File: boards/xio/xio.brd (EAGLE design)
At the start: 170 x 170 mm, 390 parts, among them U2 LAN8742A-CZ, Y1 NX3225SA-12.000MHZ-STD-CSR-1, Y2 NX3225SA-12.000MHZ-STD-CSR-1, Y3 NX3225SA-25.000MHZ-STD-CSR-1

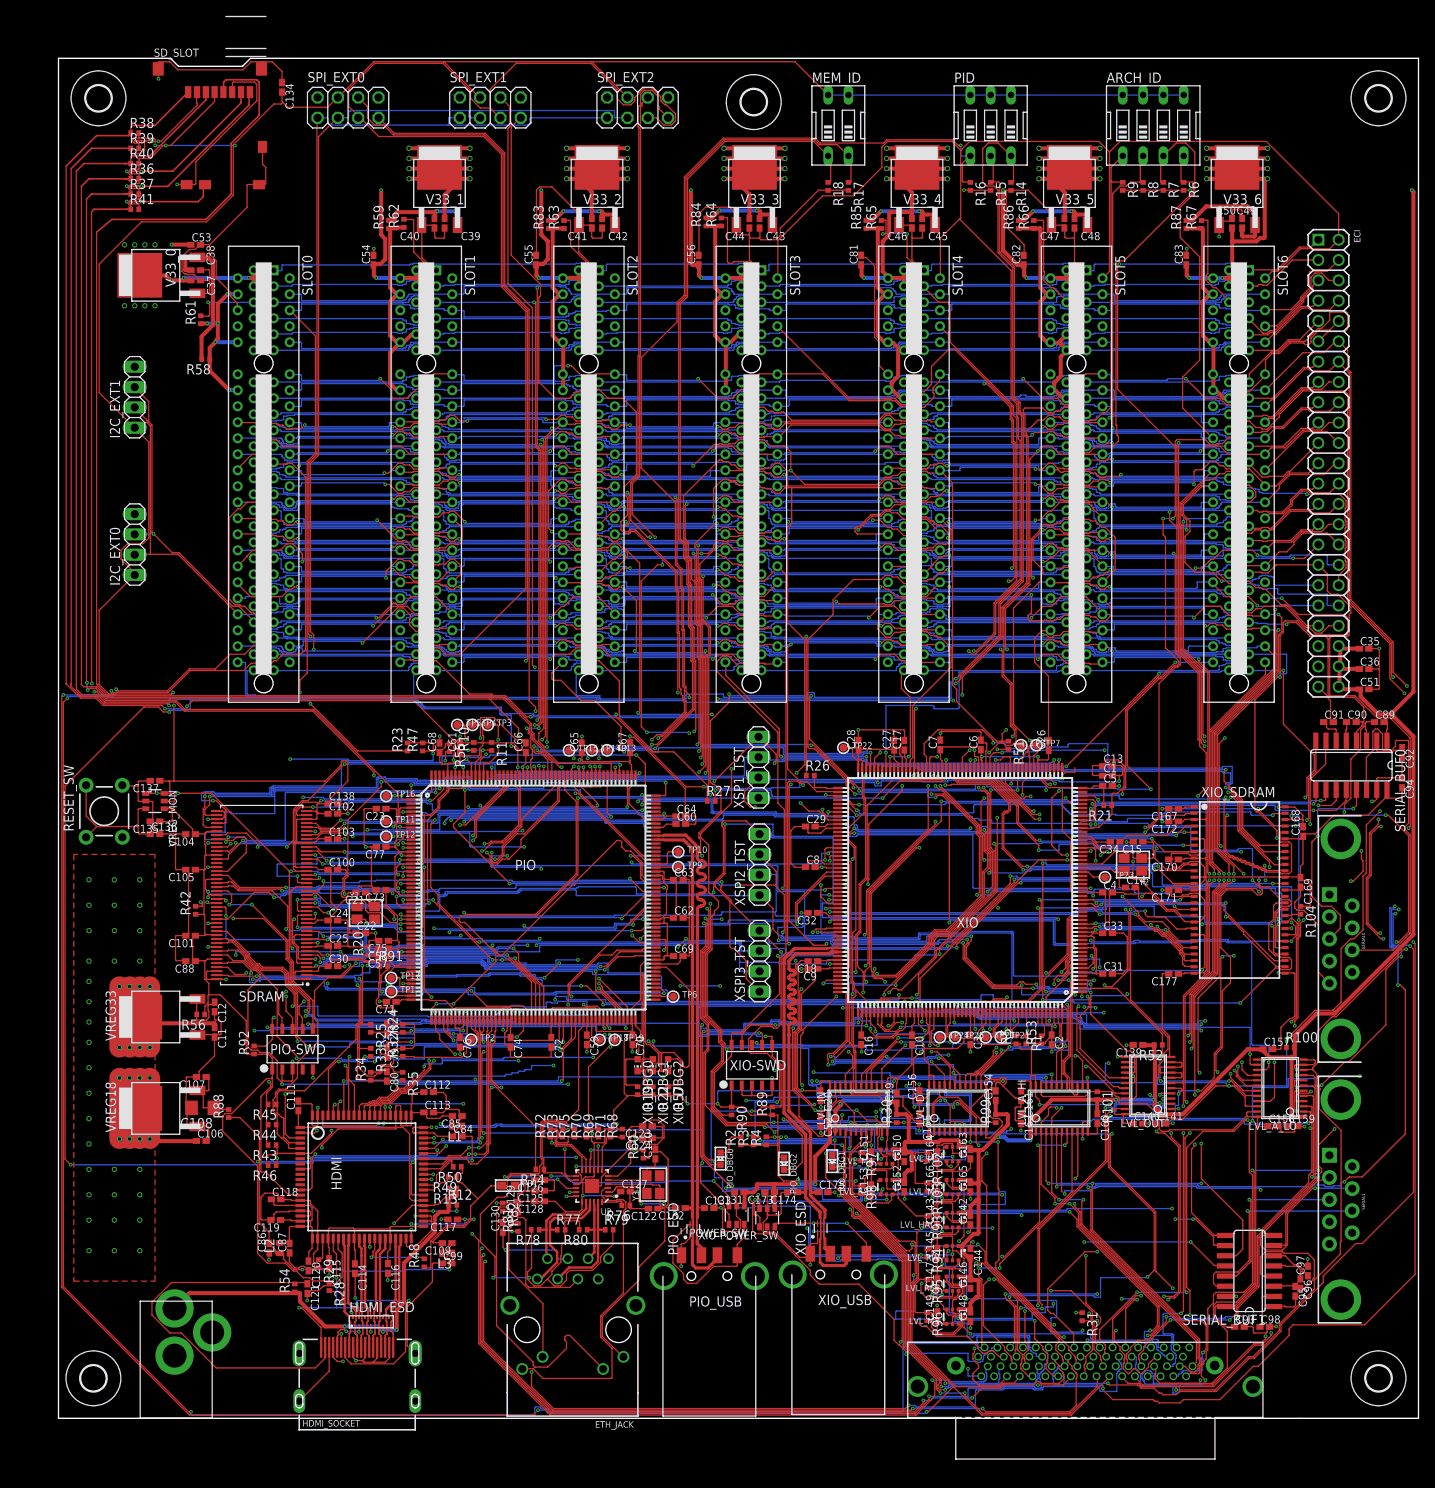
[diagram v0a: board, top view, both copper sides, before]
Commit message: Move to a 6-layer board
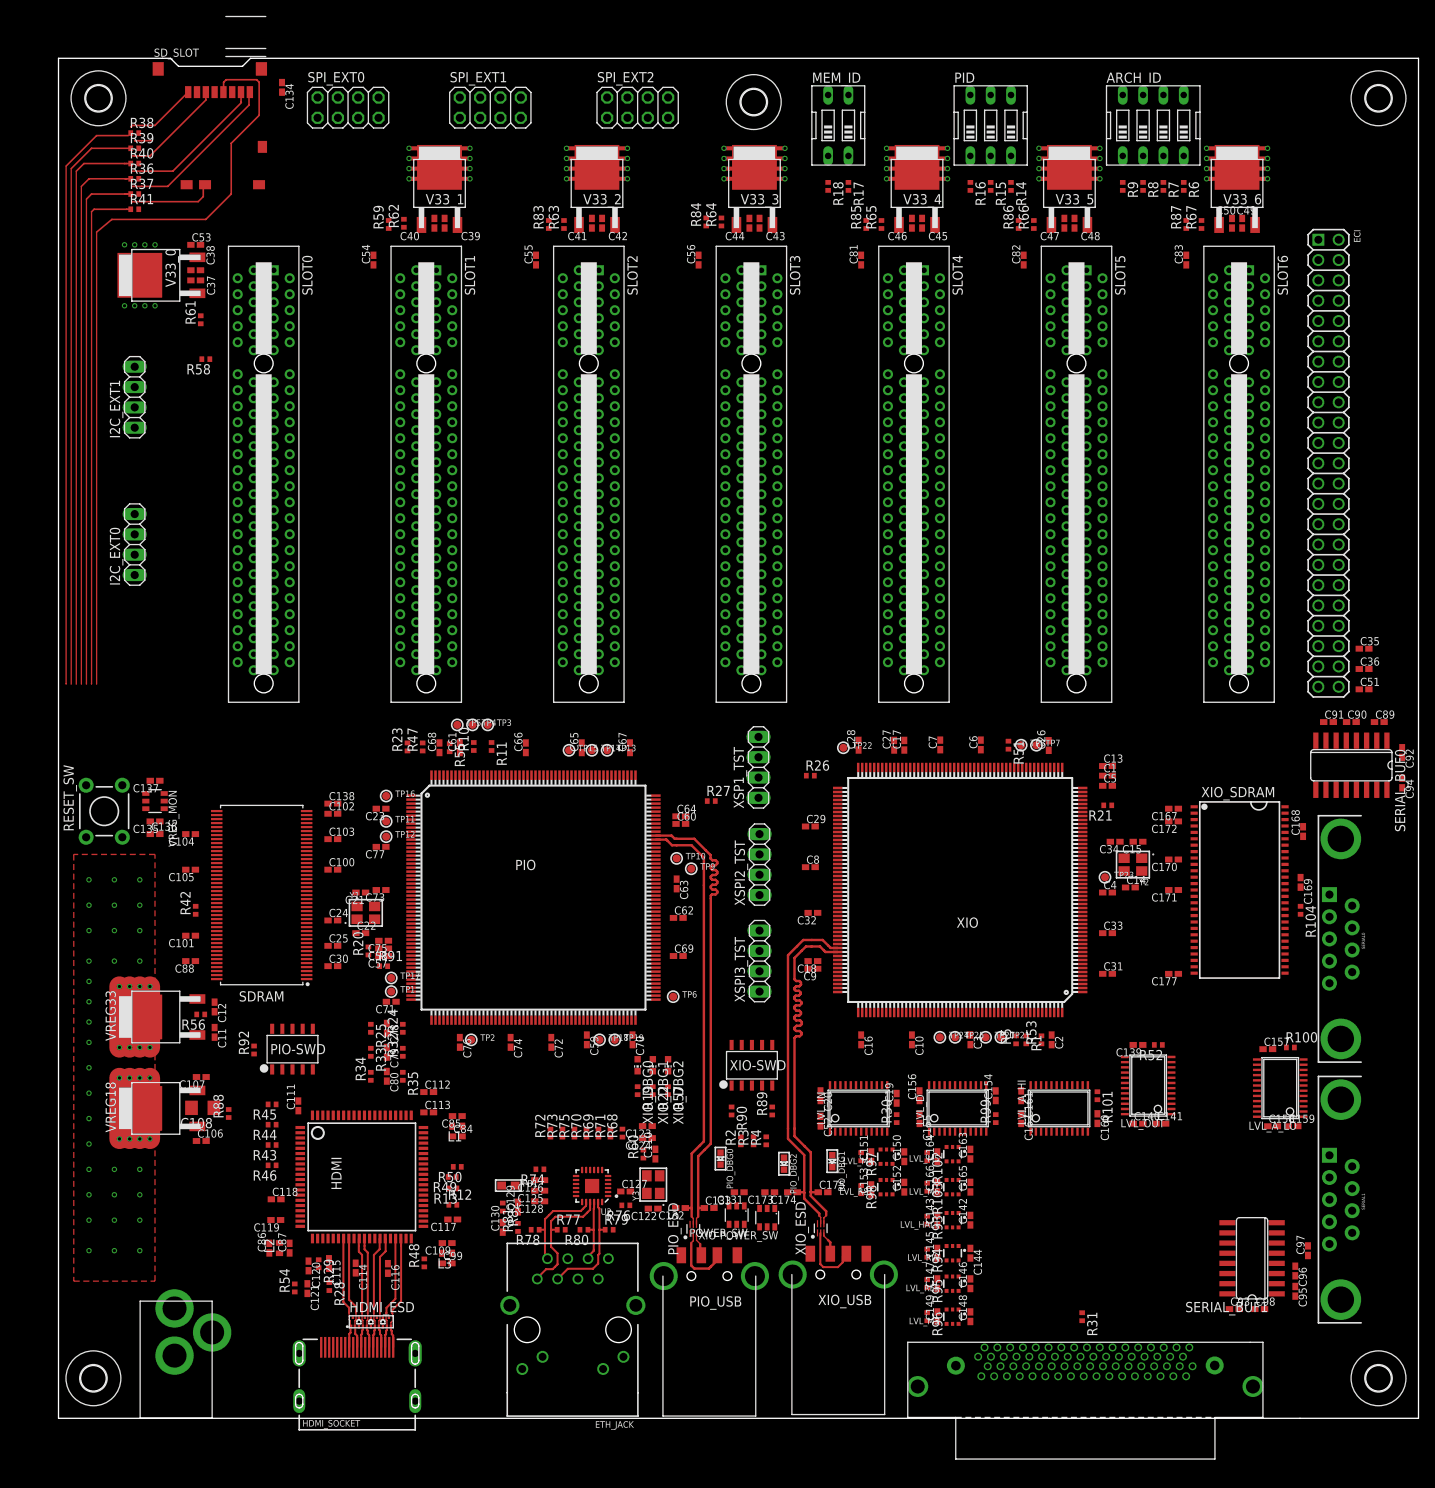
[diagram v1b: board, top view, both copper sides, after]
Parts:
- moved C97 2.54 mm to (156.2, 21.0)
- moved C93 2.31 mm to (147.0, 13.7)
- moved C98 2.31 mm to (150.2, 13.7)
- moved C96 1.71 mm to (154.6, 18.4)
- moved TP9 1.64 mm to (79.1, 68.7)
- moved SERIAL_BUF1 1.62 mm to (149.2, 20.0)
- moved TP10 0.84 mm to (77.3, 70.0)
- moved C63 0.55 mm to (77.3, 66.8), turned to 270 degrees
- moved C114 0.13 mm to (37.1, 18.8)
- moved R80 0.10 mm to (65.7, 23.6)
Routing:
- net +3V3: track 1336.9 -> 0.00 mm, vias 19 -> 0
- net GND: track 1120.3 -> 0.00 mm, vias 125 -> 0
- net +5V: track 736.1 -> 165.5 mm, vias 131 -> 104
- net VHDCI_CCTL: track 453.3 -> 0.00 mm, vias 5 -> 0
- net VHDCI_A14: track 436.6 -> 0.00 mm, vias 5 -> 0
- net !VHDCI_IRQ!: track 392.2 -> 0.00 mm, vias 6 -> 0
- net VHDCI_AUDIO_L: track 357.8 -> 0.00 mm, vias 7 -> 0
- net VHDCI_AUDIO_SIO: track 354.9 -> 0.00 mm, vias 4 -> 0
- net VHDCI_J2_5: track 353.8 -> 0.00 mm, vias 2 -> 0
- net I2C_SDA: track 349.0 -> 0.00 mm, vias 6 -> 0
- net VHDCI_J1_2: track 340.3 -> 0.00 mm, vias 3 -> 0
- net VHDCI_AUDIO_R: track 332.8 -> 0.00 mm, vias 6 -> 0
- net VHDCI_A1: track 330.8 -> 0.00 mm, vias 3 -> 0
- net VHDCI_A5: track 329.3 -> 0.00 mm, vias 11 -> 0
- net VHDCI_A11: track 328.0 -> 0.00 mm, vias 9 -> 0
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
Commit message: Latest board layout
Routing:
- net +3V3: track 0.00 -> 1208.2 mm, vias 0 -> 144
- net +5V: track 165.5 -> 732.9 mm, vias 104 -> 161
- net GND: track 0.00 -> 374.2 mm, vias 0 -> 264
- net VHDCI_AUDIO_SIO: track 0.00 -> 368.6 mm, vias 0 -> 4
- net VHDCI_AUDIO_L: track 0.00 -> 356.3 mm, vias 0 -> 12
- net VHDCI_AUDIO_R: track 0.00 -> 350.3 mm, vias 0 -> 10
- net VHDCI_A3: track 0.00 -> 333.5 mm, vias 0 -> 3
- net VHDCI_RD4: track 0.00 -> 323.5 mm, vias 0 -> 4
- net VHDCI_A7: track 0.00 -> 322.0 mm, vias 0 -> 5
- net VHDCI_RD5: track 0.00 -> 320.2 mm, vias 0 -> 5
- net VHDCI_A6: track 0.00 -> 317.0 mm, vias 0 -> 4
- net VHDCI_D1XX: track 0.00 -> 314.5 mm, vias 0 -> 5
- net VHDCI_CCTL: track 0.00 -> 313.3 mm, vias 0 -> 4
- net !VHDCI_EXSEL!: track 0.00 -> 307.7 mm, vias 0 -> 5
- net VHDCI_CLK: track 0.00 -> 306.9 mm, vias 0 -> 3
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
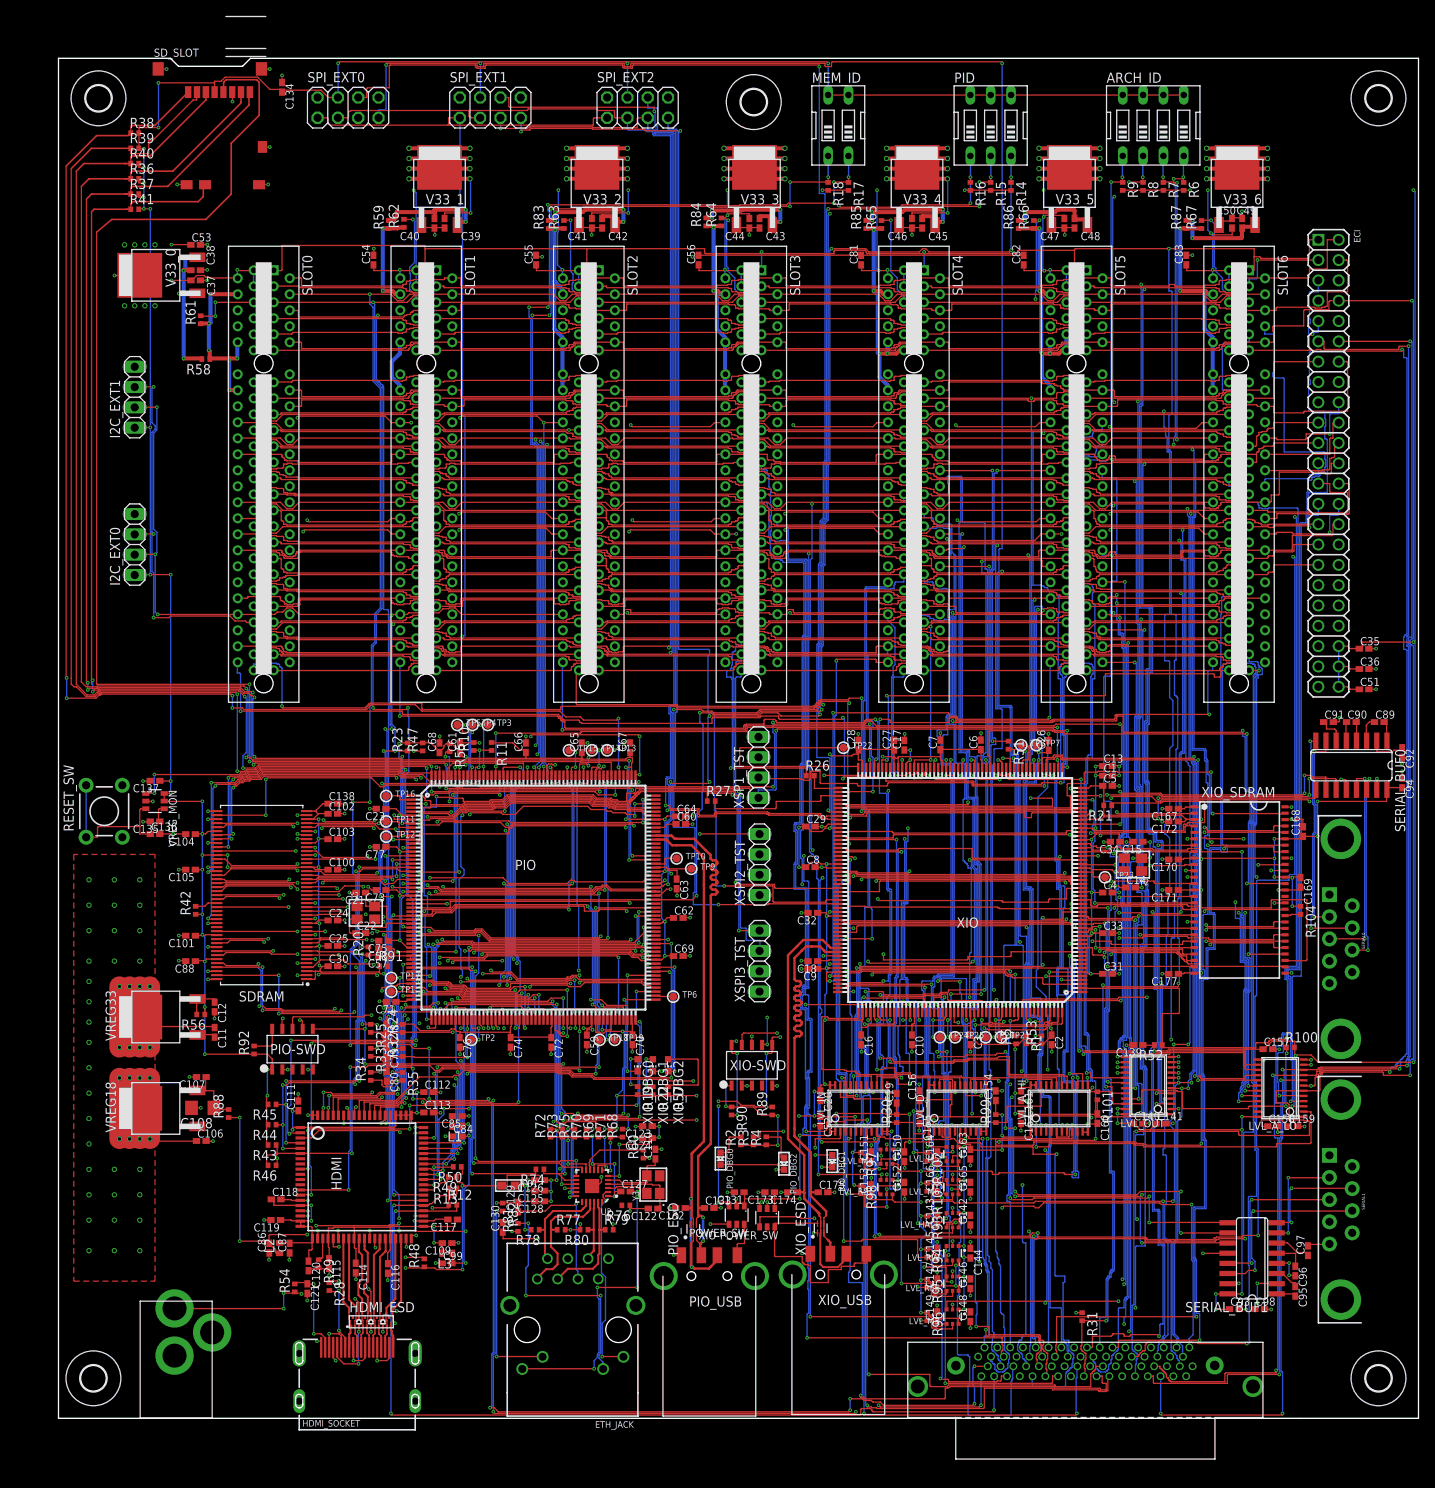
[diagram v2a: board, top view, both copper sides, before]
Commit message: Routable board
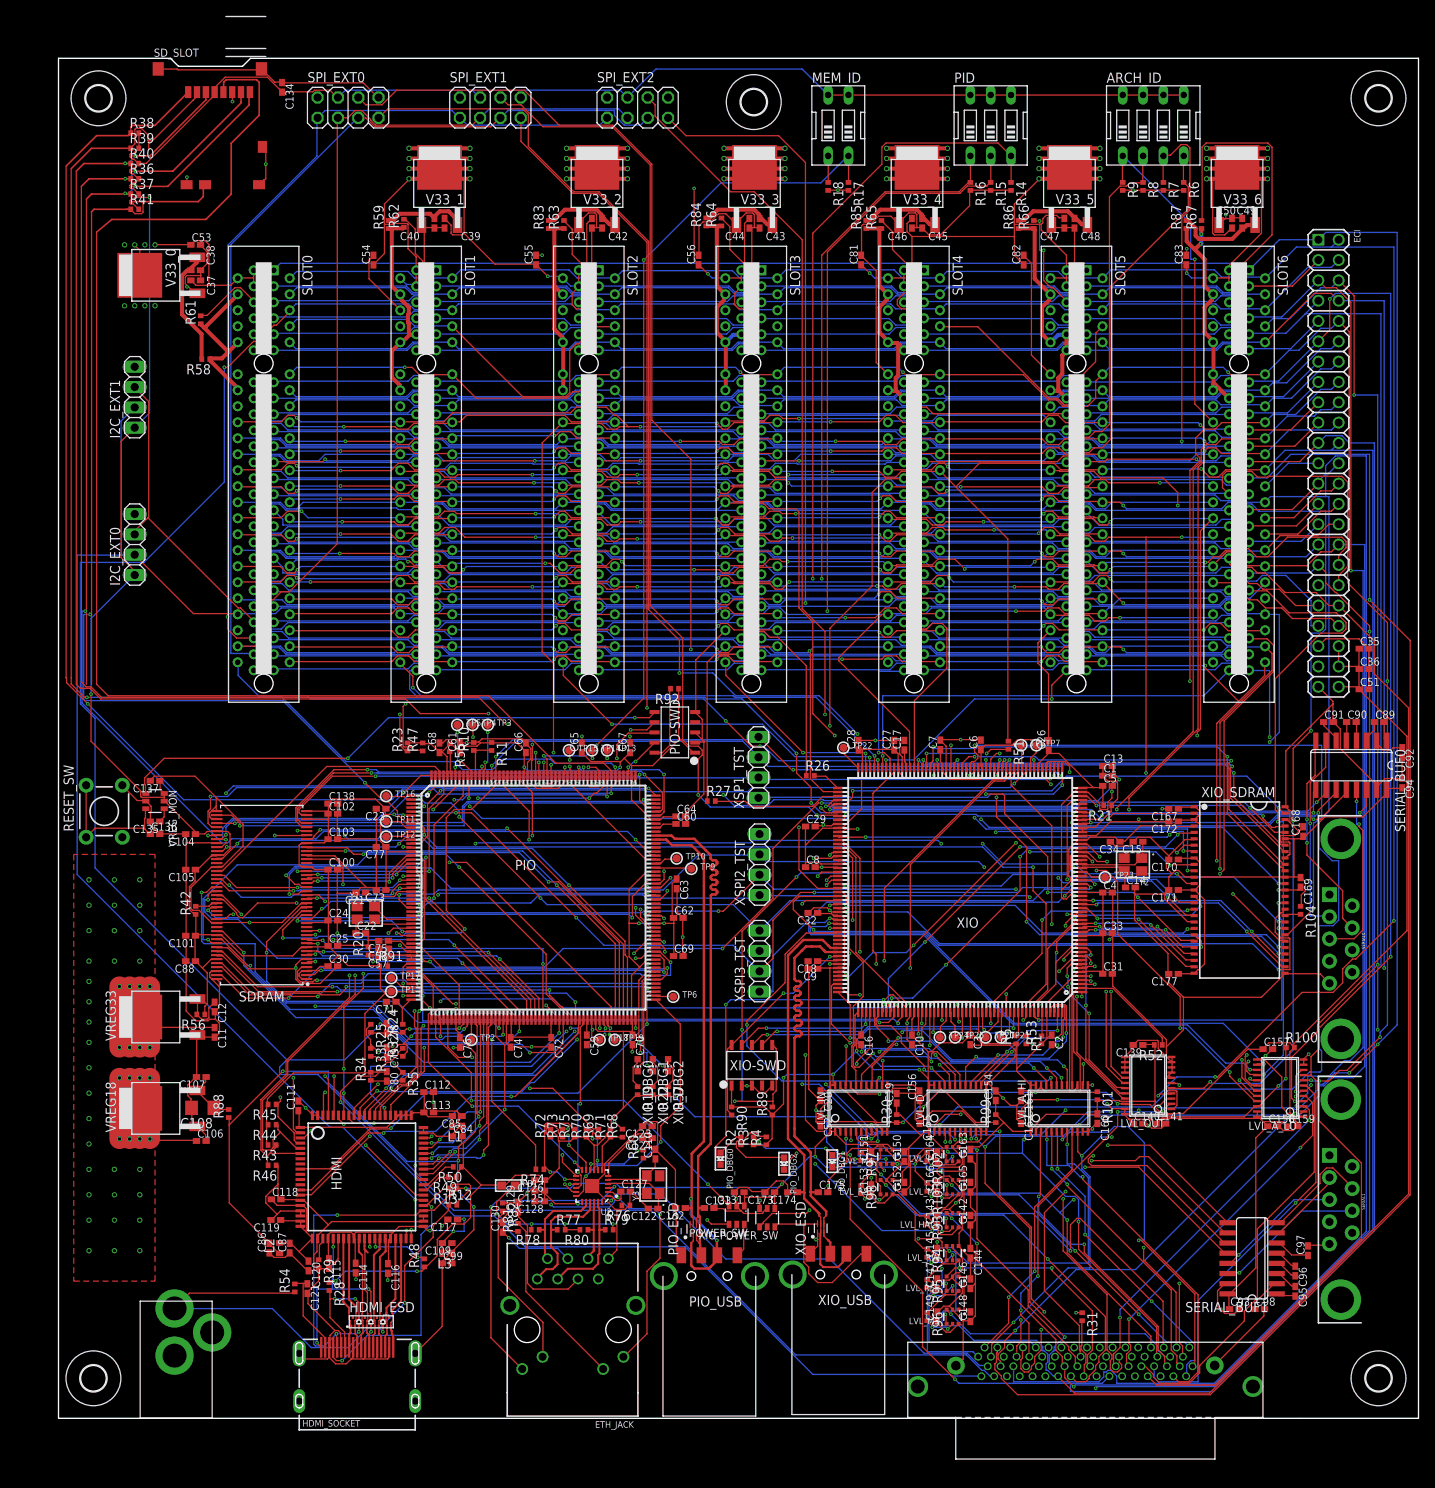
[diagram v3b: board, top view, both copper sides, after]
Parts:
- moved R92 69.3 mm to (77.0, 91.2), turned to 180 degrees
- moved PIO-SWD 62.1 mm to (77.0, 85.7), turned to 90 degrees
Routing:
- net GND: track 374.2 -> 1203.2 mm, vias 264 -> 75
- net PIO_SWDCLK: track 76.6 -> 5.61 mm
- net PIO_TX: track 66.4 -> 14.2 mm, vias 3 -> 2
- net VHDCI_COMMAND: track 253.6 -> 305.3 mm, vias 2 -> 1
- net PIO_RX: track 65.3 -> 14.0 mm
- net VHDCI_A7: track 322.0 -> 272.8 mm, vias 5 -> 1
- net VHDCI33_RSRVD6: track 92.5 -> 49.6 mm
- net SPI_IRQ7: track 210.0 -> 167.5 mm
- net VHDCI_D1XX: track 314.5 -> 273.4 mm, vias 5 -> 6
- net VHDCI_D1: track 296.3 -> 337.3 mm, vias 2 -> 1
- net VHDCI_RD5: track 320.2 -> 279.5 mm, vias 5 -> 9
- net VHDCI_A3: track 333.5 -> 292.9 mm, vias 3 -> 2
- net VHDCI_HALT: track 253.6 -> 294.2 mm, vias 3 -> 4
- net +3V3: track 1208.2 -> 1247.8 mm, vias 144 -> 23
- net VHDCI_AUDIO_L: track 356.3 -> 316.8 mm, vias 12 -> 2
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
